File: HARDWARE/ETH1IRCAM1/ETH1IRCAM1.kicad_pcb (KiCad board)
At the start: 4 copper layers, 75 x 45 mm, 107 parts, among them J201 MKDS 1,5/ 2-5,08, J301 RJ45_Wuerth_7499010121A, J401 20021111-00010T4LF, Q201 SI5618A, Q202 MMBT3904, Q501 MMBT3904, U201 TSR_1-2450, U202 TLV62568DBV, U203 TLV75530PDBV, U204 MIC5365-2.8YD5, U205 MIC5365-1.2YD5, U301 LAN8742A, U401 STM32H723VETx, U402 24LC08B-E/MS, U501 105028-1001 + Lepton 3.1R, X501 ASEMB-25.000MHZ-LY-T, Y301 NX5032GA-25, Y401 NX5032GA-16

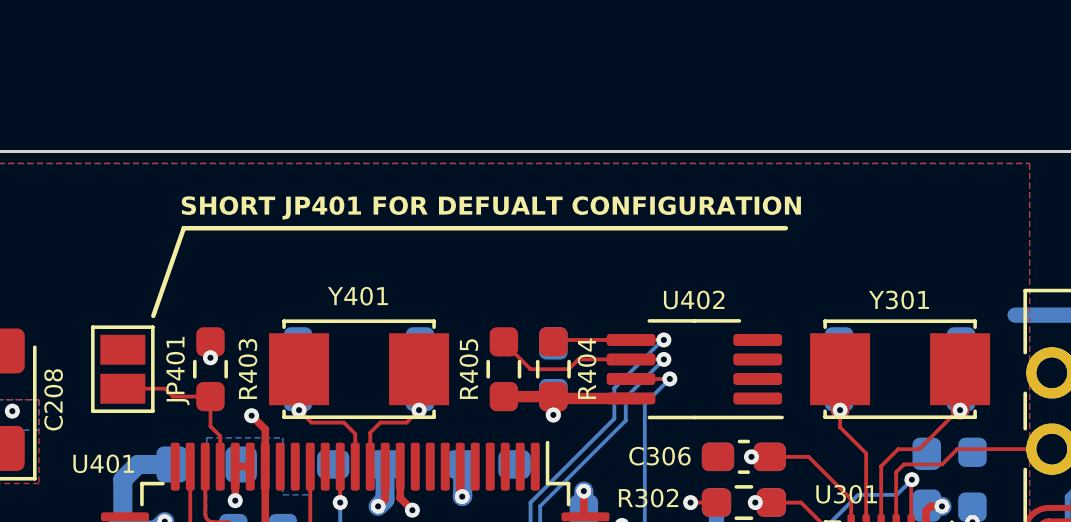
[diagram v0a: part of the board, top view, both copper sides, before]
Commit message: Bug fixes in software and PCB. Updated Readme.md file. Started SCPI documentation as a LaTex file.
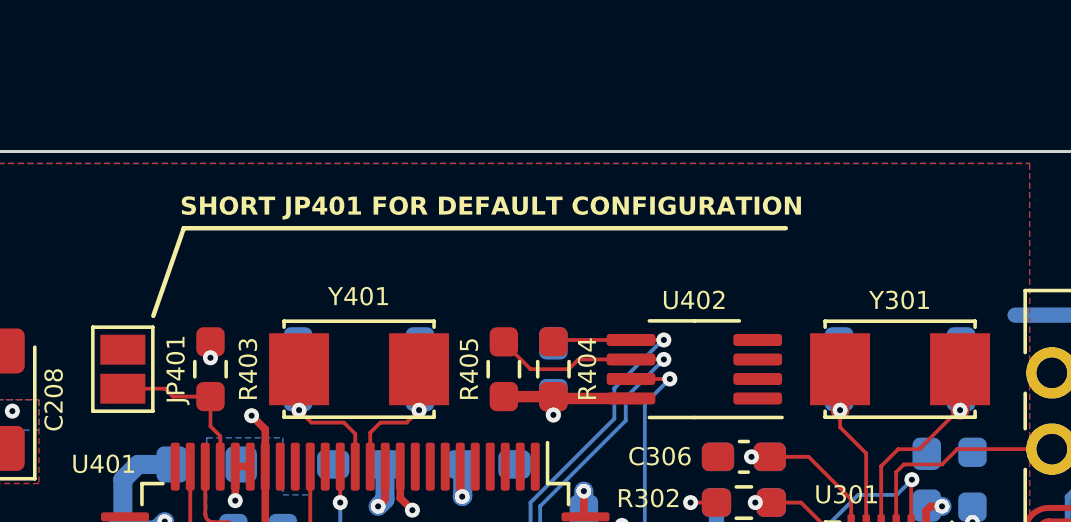
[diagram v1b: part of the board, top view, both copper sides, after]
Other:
- board text added: "SHORT JP401 FOR DEFAULT CONFIGURATION"
- board text removed: "SHORT JP401 FOR DEFUALT CONFIGURATION"
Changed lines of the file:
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@@
     (effects (font (size 0.6 0.6) (thickness 0.12) bold) (justify left bottom))
   )
-  (gr_text "SHORT JP401 FOR DEFUALT CONFIGURATION" (at 135.382 82.677) (layer "F.SilkS")
+  (gr_text "SHORT JP401 FOR DEFAULT CONFIGURATION" (at 135.382 82.677) (layer "F.SilkS")
     (effects (font (size 0.6 0.6) (thickness 0.12) bold) (justify left bottom))
   )
